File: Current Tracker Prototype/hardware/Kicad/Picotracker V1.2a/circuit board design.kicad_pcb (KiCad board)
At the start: 2 copper layers, 33.3 x 20.1 mm, 31 parts, among them J1 Conn_01x10, J2 GND, J3 3.3V, J4 ICSS Logo, J5 Conn_01x01, J6 Conn_01x01, Q1 IRLML6402, SW1 SW_Push, U1 MAX-M8C, U3 CMWX1ZZABZ-078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

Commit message: sent off designs for pcbs v1.2
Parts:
- removed J6: Conn_01x01, Connector_Wire:SolderWirePad_1x01_Drill0.8mm
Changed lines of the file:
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@@
     (tracks 319)
     (zones 0)
-    (modules 31)
+    (modules 30)
     (nets 22)
   )
@@
       (drillshape 0)
       (scaleselection 1)
-      (outputdirectory "D:/Long term storage and temp/dead weight program downloads/lora tracker outputs/loratracker v1.1a/"))
+      (outputdirectory "D:/Long term storage and temp/dead weight program downloads/lora tracker outputs/loratracker v1.2a/"))
   )
   (net 0 "")
@@
     (uvia_drill 0.1)
   )
-  (module Connector_Wire:SolderWirePad_1x01_Drill0.8mm (layer F.Cu)
-    (at 267.97 170.688)
-    (descr "Wire solder connection")
-    (tags connector)
-    (attr virtual)
-    (fp_text reference J6 (at 0 -2.54) (layer F.SilkS)
-      (effects (font (size 1 1) (thickness 0.15)))
-    )
-    (fp_text value Conn_01x01 (at 0 2.54) (layer F.Fab)
-      (effects (font (size 1 1) (thickness 0.15)))
-    )
-    (fp_line (start 1.5 1.5) (end -1.5 1.5) (layer F.CrtYd) (width 0.05))
-    (fp_line (start 1.5 1.5) (end 1.5 -1.5) (layer F.CrtYd) (width 0.05))
-    (fp_line (start -1.5 -1.5) (end -1.5 1.5) (layer F.CrtYd) (width 0.05))
-    (fp_line (start -1.5 -1.5) (end 1.5 -1.5) (layer F.CrtYd) (width 0.05))
-    (fp_text user %R (at 0 0) (layer F.Fab)
-      (effects (font (size 1 1) (thickness 0.15)))
-    )
-    (pad 1 thru_hole circle (at 0 0) (size 1.99898 1.99898) (drill 0.8001) (layers *.Cu *.Mask)
-      (net 1 GND))
-  )
   (module Resistor_SMD:R_0402_1005Metric (layer F.Cu)

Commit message: connect gps to usart2 port
pull gps ddc and uart pins out to side test points
connect stm32 reset line to vcc via resistor
connect stm32 to gps via usart2
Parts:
- removed C1: 100nF, Capacitor_SMD:C_0402_1005Metric
- removed R7: 100K, Resistor_SMD:R_0402_1005Metric
- removed SW1: SW_Push, flight-computer:EVPAWCD4A
- added J6: Conn_01x01, Connector_Wire:SolderWirePad_1x01_Drill0.8mm, F.Cu at (268.0, 171.3)
- added R9: 10K, Resistor_SMD:R_0402_1005Metric, F.Cu at (267.8, 175.4)
- added TP1: TestPoint, TestPoint:TestPoint_Pad_D2.0mm, F.Cu at (248.0, 175.6)
- added TP2: TestPoint, TestPoint:TestPoint_Pad_D2.0mm, F.Cu at (243.1, 181.9)
- added TP3: TestPoint, TestPoint:TestPoint_Pad_D2.0mm, F.Cu at (237.1, 175.5)
- added TP4: TestPoint, TestPoint:TestPoint_Pad_D2.0mm, F.Cu at (247.1, 181.9)
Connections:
- U1 pad 16: /I2C1_SDA -> (no net)
- U1 pad 17: /I2C1_SCL -> (no net)
- U1 pad 2: (no net) -> /USART2_RX
- U1 pad 3: (no net) -> /USART2_TX
- U1 pad 9: +3V3 -> (no net)
- U3 pad 22: (no net) -> /LED
- U3 pad 23: /SWITCH -> /USART2_RX
- U3 pad 24: /LED -> /USART2_TX
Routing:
- net /USART2_RX: track 0.00 -> 27.7 mm, vias 0 -> 2
- net /USART2_TX: track 0.00 -> 25.4 mm, vias 0 -> 2
- net /SWITCH: track 6.56 -> 0.00 mm
- net /USART1_TX: track 27.6 -> 30.6 mm
- net /GPS_TIMEPULSE: track 16.1 -> 18.6 mm
- net /USART1_RX: track 27.7 -> 30.2 mm
- net +3V3: track 82.0 -> 79.6 mm
- net /RESET: track 7.86 -> 9.70 mm
- net /I2C1_SDA: track 34.3 -> 33.1 mm
- net /I2C1_SCL: track 31.9 -> 30.8 mm
- net /LED: track 2.62 -> 3.74 mm
- net /GPS_EXTINT: track 17.9 -> 19.0 mm
- net GND: vias 40 -> 36

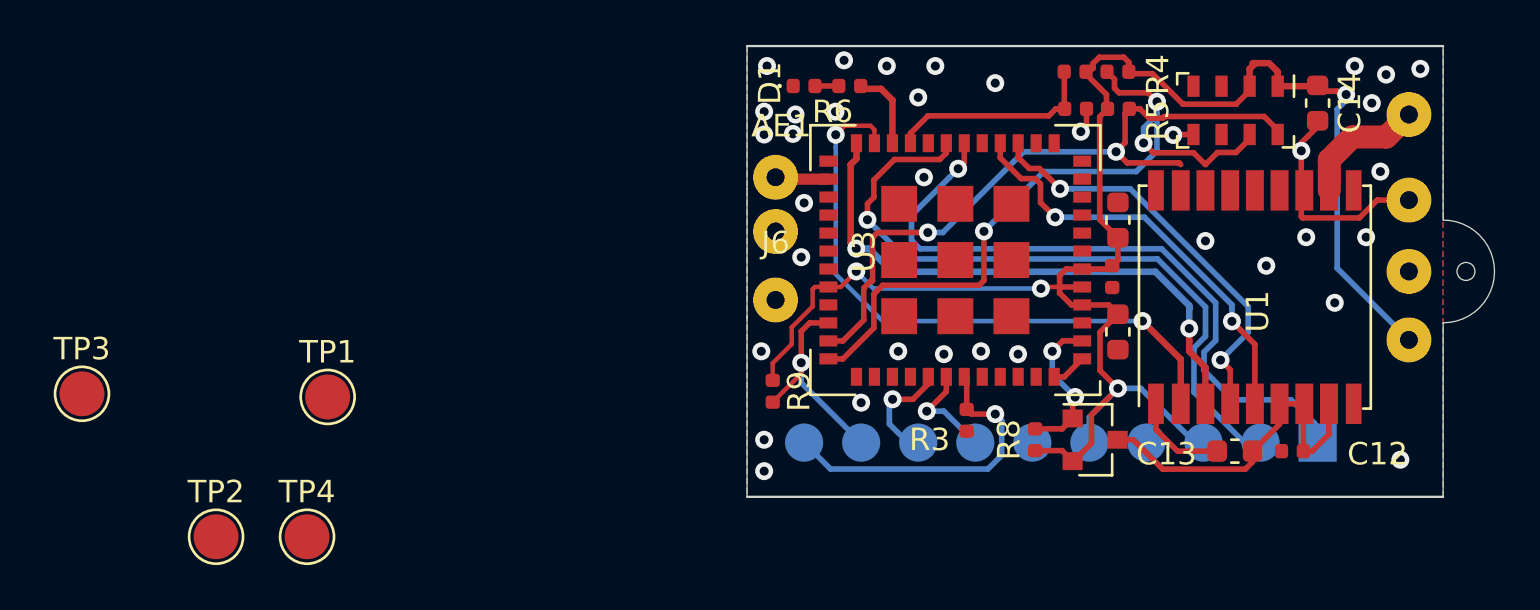
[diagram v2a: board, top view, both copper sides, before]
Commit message: put in the test points
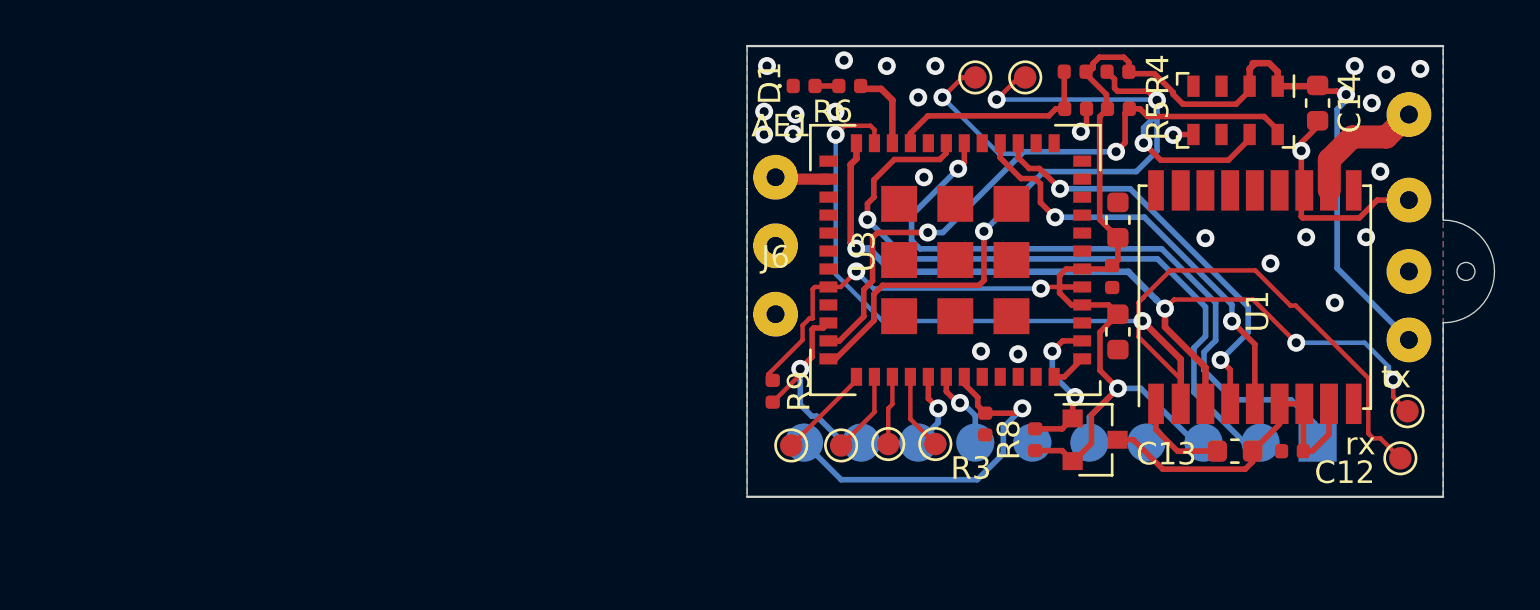
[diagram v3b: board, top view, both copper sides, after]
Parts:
- added TP5: TestPoint, TestPoint:TestPoint_Pad_D1.0mm, F.Cu at (268.7, 177.8)
- added TP6: TestPoint, TestPoint:TestPoint_Pad_D1.0mm, F.Cu at (275.1, 177.7)
- added TP7: TestPoint, TestPoint:TestPoint_Pad_D1.0mm, F.Cu at (273.0, 177.7)
- added TP8: TestPoint, TestPoint:TestPoint_Pad_D1.0mm, F.Cu at (270.9, 177.8)
- TP3, TP4: footprint TestPoint:TestPoint_Pad_D2.0mm -> TestPoint:TestPoint_Pad_D1.0mm
- rx: renamed from TP1; footprint TestPoint:TestPoint_Pad_D2.0mm -> TestPoint:TestPoint_Pad_D1.0mm
- tx: renamed from TP2; footprint TestPoint:TestPoint_Pad_D2.0mm -> TestPoint:TestPoint_Pad_D1.0mm
- moved tx 53.3 mm to (296.1, 176.3)
- moved rx 47.8 mm to (295.8, 178.4)
- moved TP3 42.2 mm to (276.9, 161.4)
- moved TP4 37.9 mm to (279.1, 161.4)
- moved R3 0.84 mm to (277.3, 176.8)
- moved J5 0.63 mm to (268.0, 168.9)
- moved J6 0.63 mm to (268.0, 172.0)
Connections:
- U3 pad 37: (no net) -> Net-(TP5-Pad1)
- U3 pad 38: (no net) -> Net-(TP8-Pad1)
- U3 pad 39: (no net) -> Net-(TP7-Pad1)
- U3 pad 40: (no net) -> Net-(TP6-Pad1)
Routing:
- net /USART2_RX: track 27.7 -> 50.1 mm
- net /USART2_TX: track 25.4 -> 38.4 mm, vias 2 -> 4
- net /I2C1_SDA: track 33.1 -> 41.6 mm, vias 3 -> 4
- net Net-(TP5-Pad1): track 0.00 -> 4.26 mm
- net Net-(TP8-Pad1): track 0.00 -> 3.67 mm
- net Net-(TP6-Pad1): track 0.00 -> 3.45 mm
- net /I2C1_SCL: track 30.8 -> 33.9 mm, vias 2 -> 3
- net Net-(TP7-Pad1): track 0.00 -> 3.07 mm
- net /BOOT0: track 14.3 -> 16.1 mm
- net /SWDIO: track 4.98 -> 3.48 mm
- net /SWCLK: track 4.63 -> 3.59 mm
- net GND: vias 36 -> 26

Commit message: put in test point to switched gps power supply
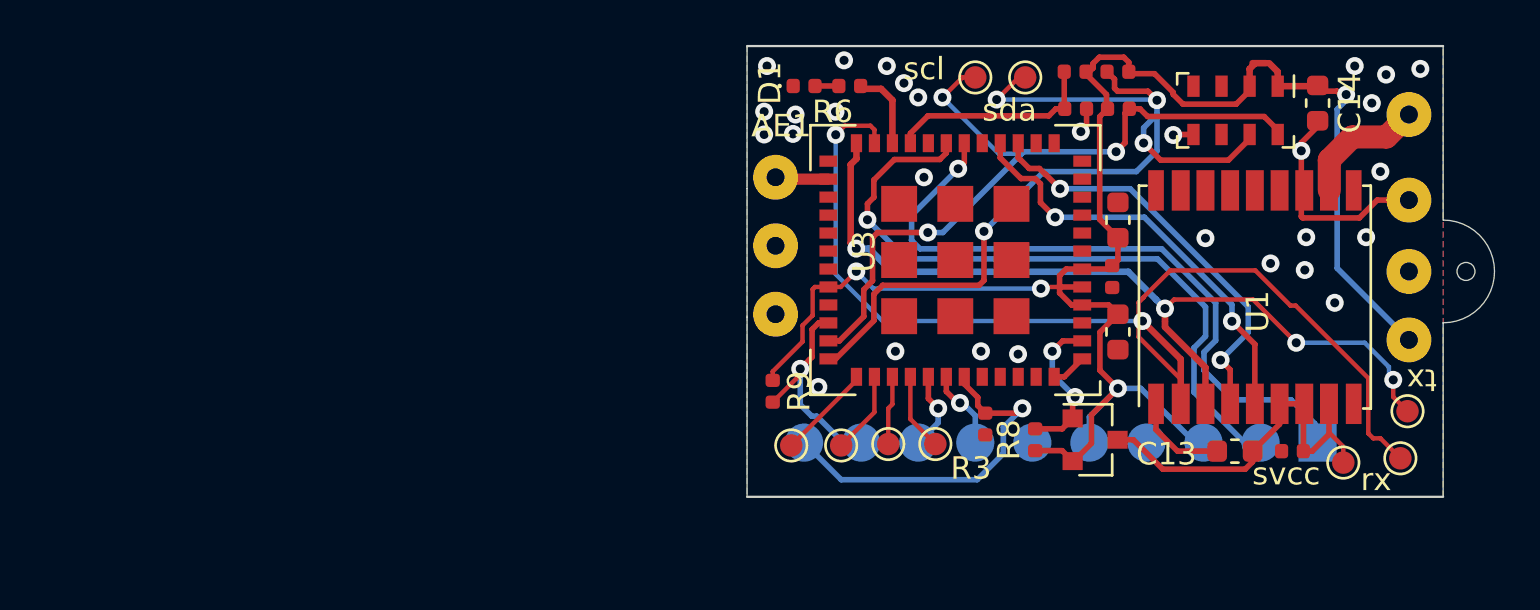
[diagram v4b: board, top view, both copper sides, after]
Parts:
- added TP9: TestPoint, TestPoint:TestPoint_Pad_D1.0mm, F.Cu at (293.2, 178.6)
- renumbered rx to TP1, tx to TP2
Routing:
- net Net-(C12-Pad1): track 15.8 -> 18.7 mm
- net GND: vias 26 -> 29
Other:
- board text added: "rx"
- board text added: "scl"
- board text added: "sda"
- board text added: "svcc"
- board text added: "tx"

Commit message: update annotation
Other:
- board text added: "PicoTracker LoRa V1.3a Imperial College Space Society Medad Newman, Richard Ibbotson August 2020"
- board text removed: "PicoTracker LoRa V1.2a Imperial College Space Society Medad Newman, Richard Ibbotson Feb 2020"
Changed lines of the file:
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@@
   )
   (layers
-    (0 F.Cu signal)
+    (0 F.Cu signal hide)
     (31 B.Cu signal hide)
     (32 B.Adhes user hide)
@@
     (34 B.Paste user hide)
     (35 F.Paste user hide)
-    (36 B.SilkS user hide)
-    (37 F.SilkS user)
+    (36 B.SilkS user)
+    (37 F.SilkS user hide)
     (38 B.Mask user hide)
     (39 F.Mask user hide)
@@
     (add_net "Net-(C12-Pad1)")
     (add_net "Net-(D1-Pad2)")
-    (add_net "Net-(SolarCellMount1-Pad1)")
     (add_net "Net-(TP5-Pad1)")
     (add_net "Net-(TP6-Pad1)")
     (add_net "Net-(TP7-Pad1)")
     (add_net "Net-(TP8-Pad1)")
-    (add_net "Net-(U1-Pad13)")
-    (add_net "Net-(U1-Pad14)")
-    (add_net "Net-(U1-Pad15)")
-    (add_net "Net-(U1-Pad16)")
-    (add_net "Net-(U1-Pad17)")
-    (add_net "Net-(U1-Pad18)")
-    (add_net "Net-(U1-Pad9)")
-    (add_net "Net-(U3-Pad10)")
-    (add_net "Net-(U3-Pad11)")
-    (add_net "Net-(U3-Pad12)")
-    (add_net "Net-(U3-Pad13)")
-    (add_net "Net-(U3-Pad14)")
-    (add_net "Net-(U3-Pad17)")
-    (add_net "Net-(U3-Pad20)")
-    (add_net "Net-(U3-Pad28)")
-    (add_net "Net-(U3-Pad29)")
-    (add_net "Net-(U3-Pad30)")
-    (add_net "Net-(U3-Pad31)")
-    (add_net "Net-(U3-Pad33)")
-    (add_net "Net-(U3-Pad45)")
-    (add_net "Net-(U3-Pad46)")
-    (add_net "Net-(U3-Pad47)")
-    (add_net "Net-(U3-Pad8)")
-    (add_net "Net-(U3-Pad9)")
-    (add_net "Net-(U6-Pad6)")
   )
   (net_class Power ""
@@
     (effects (font (size 1 1) (thickness 0.15)))
   )
-  (gr_text "PicoTracker LoRa V1.2a\nImperial College Space Society\nMedad Newman, Richard Ibbotson \nFeb 2020" (at 281.559 169.164) (layer B.SilkS)
+  (gr_text "PicoTracker LoRa V1.3a\nImperial College Space Society\nMedad Newman, Richard Ibbotson \nAugust 2020" (at 281.559 169.164) (layer B.SilkS)
     (effects (font (size 1 1) (thickness 0.15)) (justify mirror))
   )

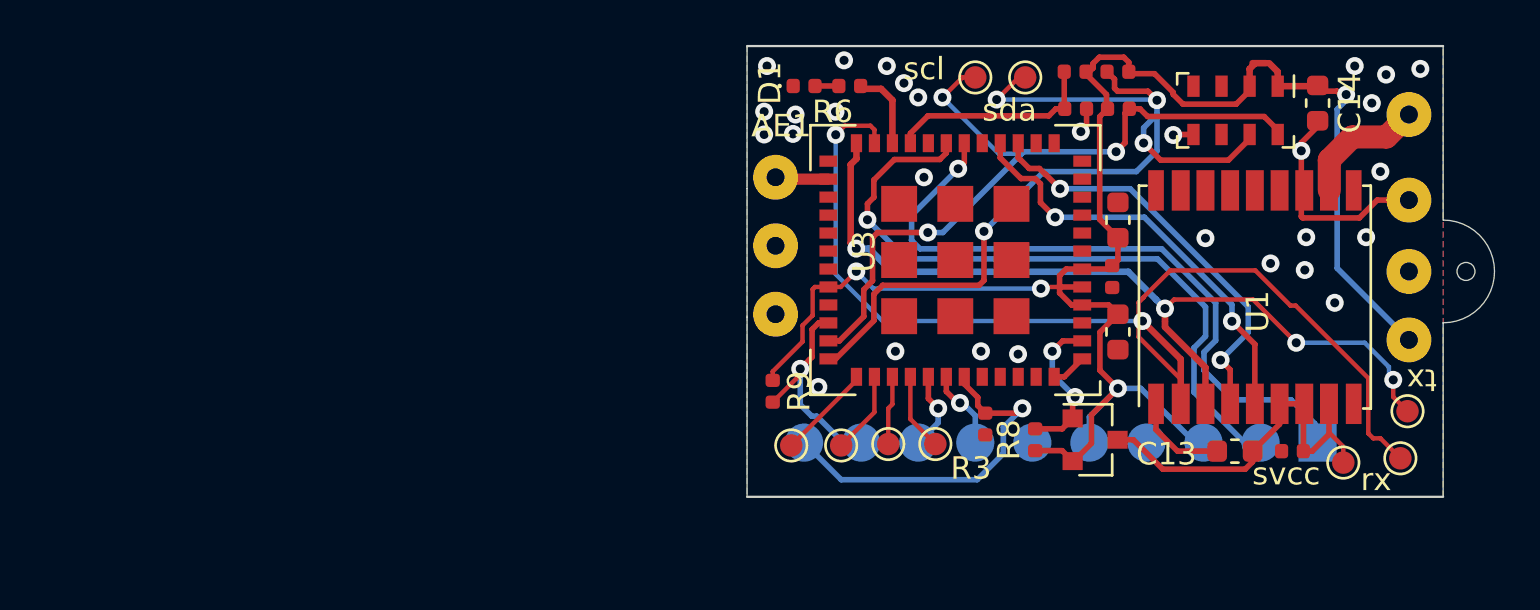
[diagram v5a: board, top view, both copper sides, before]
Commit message: put in solder jumper for uart. Connected i2c as well
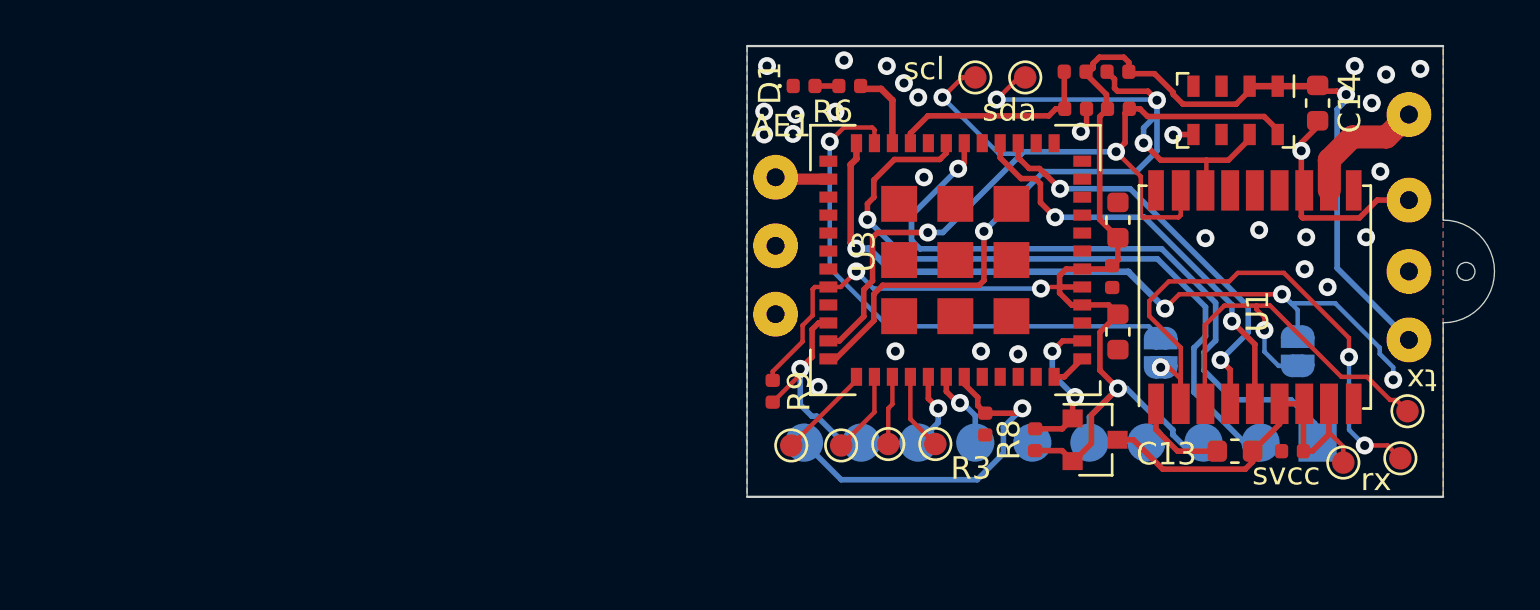
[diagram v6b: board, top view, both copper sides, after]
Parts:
- added JP1: SolderJumper_2_Open, Jumper:SolderJumper-2_P1.3mm_Open_RoundedPad1.0x1.5mm, B.Cu at (291.2, 173.6)
- added JP2: SolderJumper_2_Open, Jumper:SolderJumper-2_P1.3mm_Open_RoundedPad1.0x1.5mm, B.Cu at (285.1, 173.7)
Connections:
- TP1 pad 1: /USART2_RX -> Net-(JP2-Pad2)
- TP2 pad 1: /USART2_TX -> Net-(JP1-Pad2)
- U1 pad 16: (no net) -> /I2C1_SDA
- U1 pad 17: (no net) -> /I2C1_SCL
- U1 pad 2: /USART2_RX -> Net-(JP2-Pad2)
- U1 pad 3: /USART2_TX -> Net-(JP1-Pad2)
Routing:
- net /USART2_RX: track 50.1 -> 24.5 mm, vias 2 -> 1
- net Net-(JP2-Pad2): track 0.00 -> 24.9 mm, vias 0 -> 3
- net Net-(JP1-Pad2): track 0.00 -> 18.8 mm, vias 0 -> 1
- net /I2C1_SCL: track 33.9 -> 40.1 mm
- net /USART2_TX: track 38.4 -> 34.4 mm
- net +3V3: track 79.7 -> 78.1 mm
- net /I2C1_SDA: track 41.6 -> 43.0 mm
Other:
- board text added: "PicoTracker LoRa V1.3a Imperial College Space Society Medad Newman, Richard Ibbotson September 2020"
- board text removed: "PicoTracker LoRa V1.3a Imperial College Space Society Medad Newman, Richard Ibbotson August 2020"

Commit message: changed the lora antenna pad to rectangular
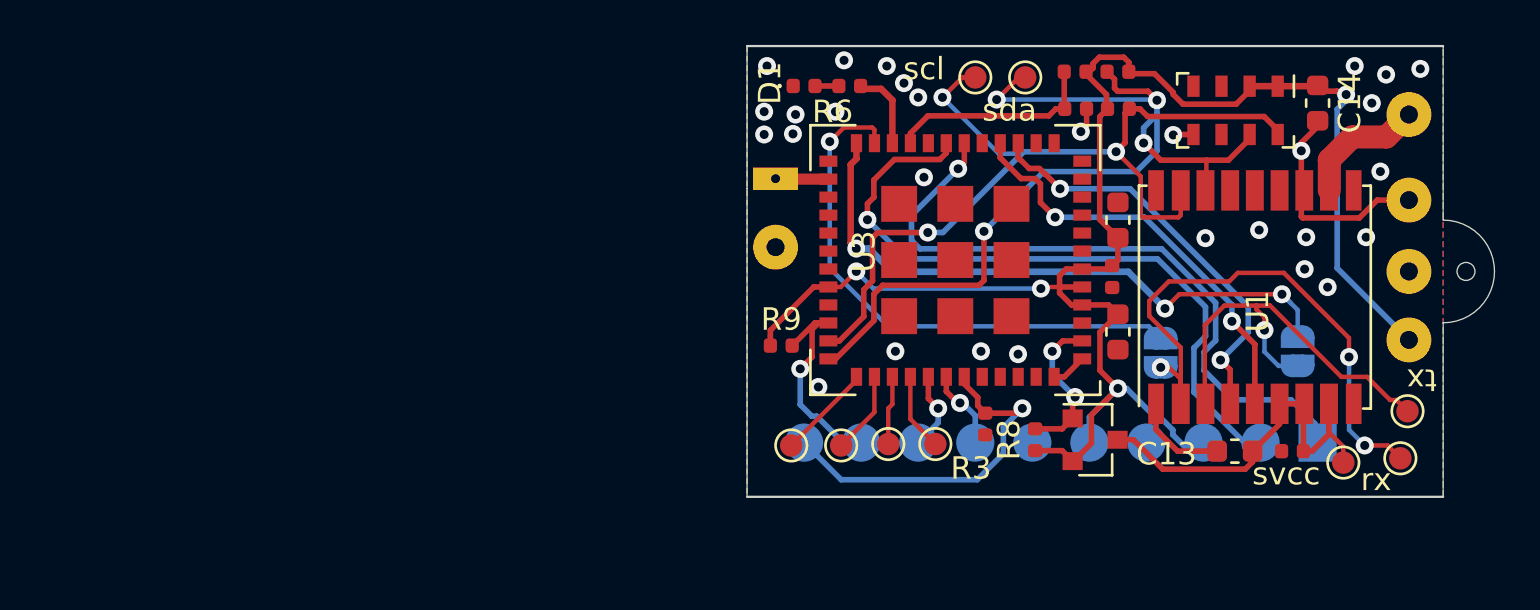
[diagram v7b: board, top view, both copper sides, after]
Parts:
- removed J6: Conn_01x01, Connector_Wire:SolderWirePad_1x01_Drill0.8mm
- AE1: footprint Connector_Wire:SolderWirePad_1x01_Drill0.8mm -> pico_tracker:SolderWirePad_1x01_Drill0.8mm_square
- moved R9 2.07 mm to (268.2, 173.4), turned to 0 degrees
- moved AE1 0.06 mm to (268.0, 165.9)
- moved J5 0.06 mm to (268.0, 169.0)
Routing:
- net /USART2_TX: track 34.4 -> 28.0 mm, vias 4 -> 3
- net +3V3: track 78.1 -> 76.7 mm

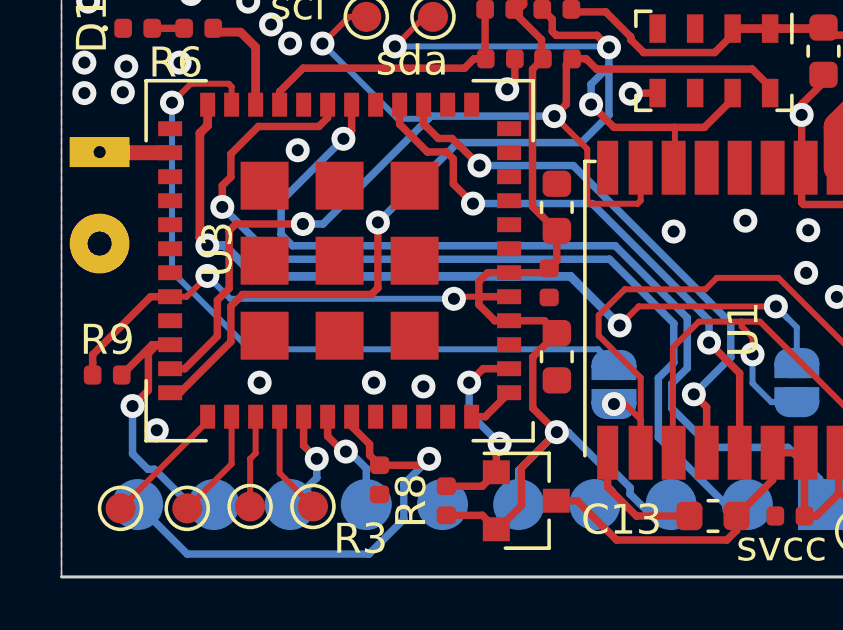
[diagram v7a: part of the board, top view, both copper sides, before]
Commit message: made seperate custom abz foot print
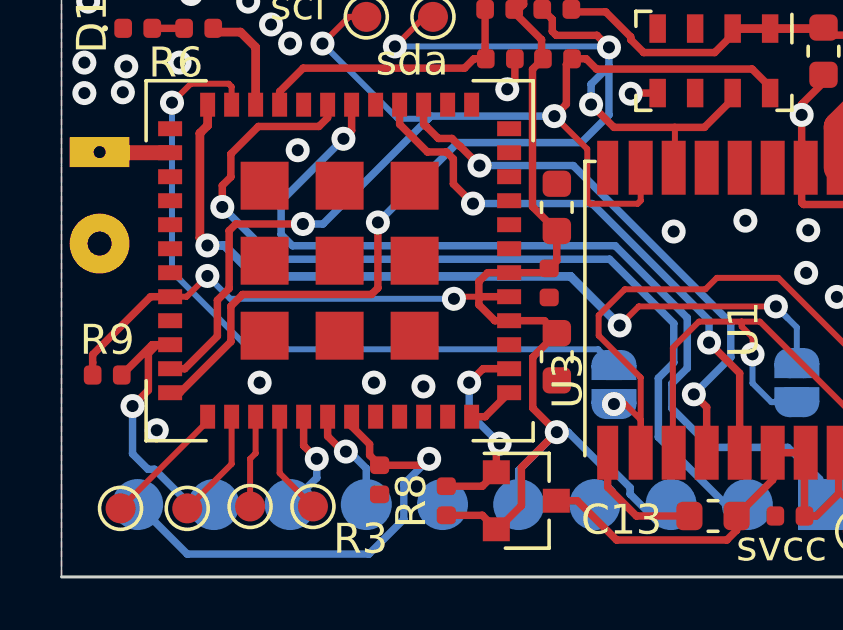
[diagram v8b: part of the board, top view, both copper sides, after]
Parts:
- U3: footprint RF_Module:CMWX1ZZABZ -> pico_tracker:CMWX1ZZABZ_custom
